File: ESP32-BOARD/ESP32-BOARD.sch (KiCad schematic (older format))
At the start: 160 parts, among them J101 Screw_Terminal_01x08, J102 Screw_Terminal_01x08, J103 Screw_Terminal_01x08, J104 Screw_Terminal_01x08, J105 Input_01x02, J106 Screw_Terminal_01x04, J120 Conn_01x07_Male, Q101 BT136-600, Q102 BT136-600, Q103 BT136-600, Q104 BT136-600, U101 LM358, U102 LM358, U103 LM2596S-ADJ, U104 LM2596S-ADJ, U105 TLP290-4, U106 TLP290-4, U107 KAQY214S, U108 KAQY214S, U109 MOC3023S, U110 MOC3023S, U111 MOC3023S, U112 MOC3023S, U113 SIM800L, U114 ESP32-dev-board

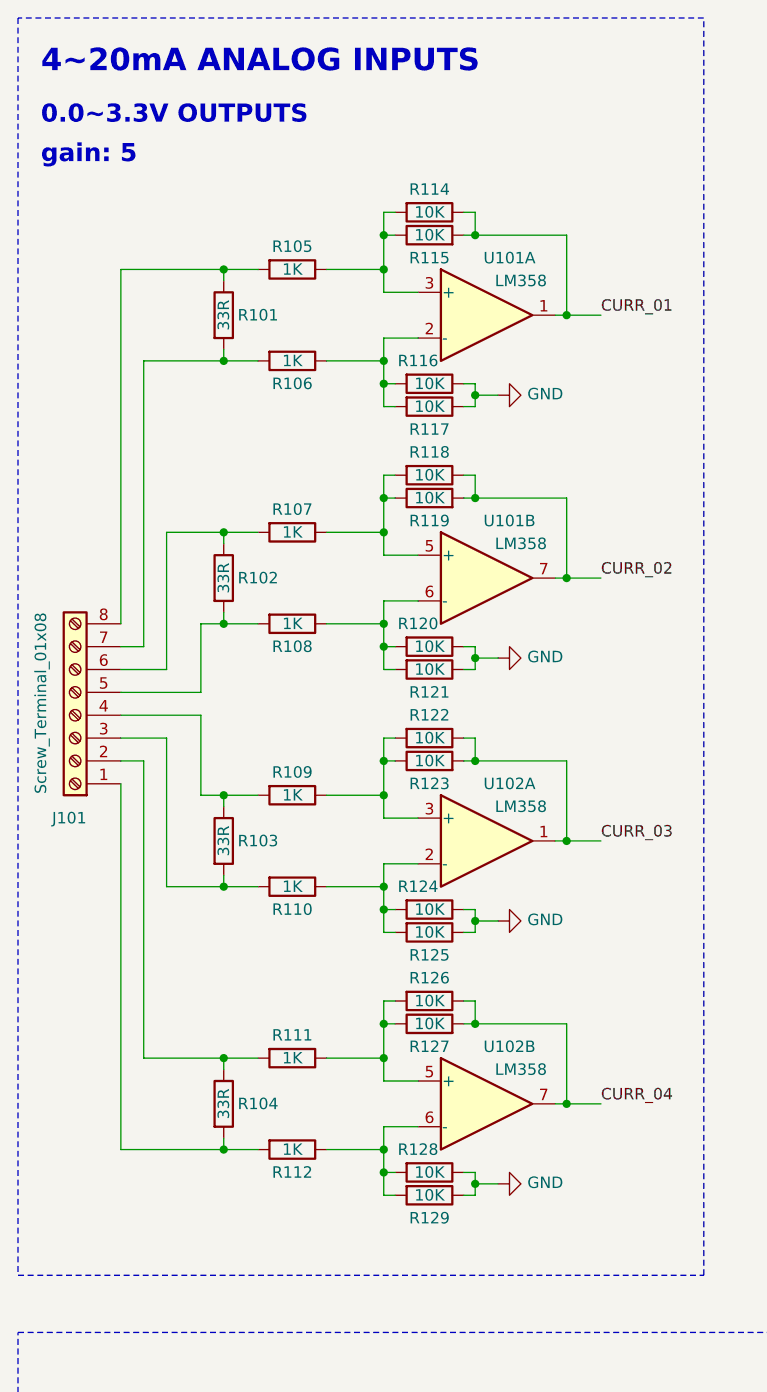
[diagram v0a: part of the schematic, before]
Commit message: changes made on the analog inputs
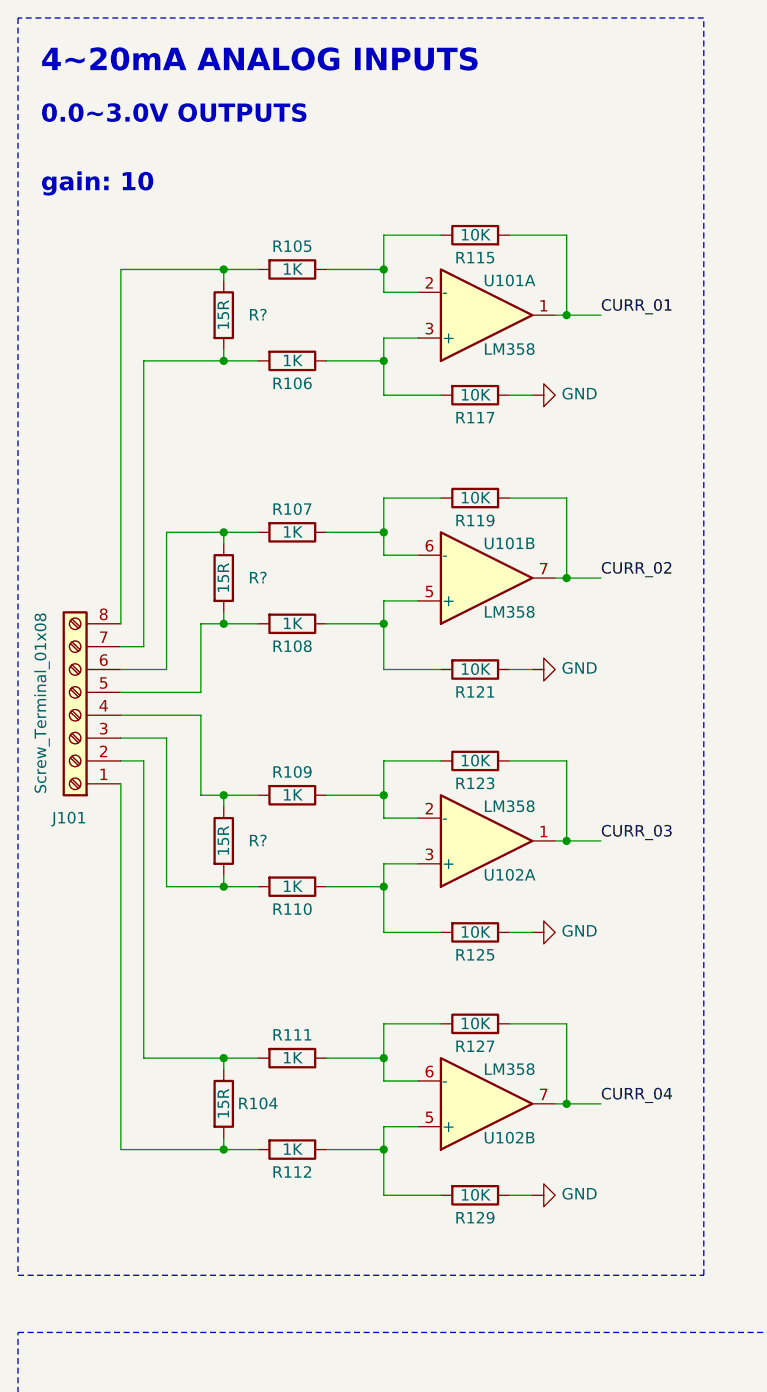
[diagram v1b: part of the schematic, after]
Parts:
- removed R101, R102, R103: 33R, Resistor_SMD:R_0805_2012Metric, symbol Device:R
- removed R114, R116, R118, R120, R122, R124, R126, R128: 10K, Resistor_SMD:R_0805_2012Metric, symbol Device:R
- added R? (x3): 15R, Resistor_SMD:R_0805_2012Metric, symbol Device:R
- R104: value 33R -> 15R; LCSC C17634 -> C17480
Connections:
- net at R106.1, R117.2: now also U101.3 (+); no longer U101.2 (-)
- net at R105.1, R115.1: now also U101.2 (-); no longer U101.3 (+)
- net at R107.1, R119.1: now also U101.6 (-); no longer U101.5 (+)
- net at R108.1, R121.2: now also U101.5 (+); no longer U101.6 (-)
- net at J101.8 (Pin_8), R105.2: now also R?.1
- net at J101.7 (Pin_7), R106.2: now also R?.2
- net at J101.6 (Pin_6), R107.2: now also R?.1
- net at J101.5 (Pin_5), R108.2: now also R?.2
- net at R110.1, R125.2: now also U102.3 (+); no longer U102.2 (-)
- net at R109.1, R123.1: now also U102.2 (-); no longer U102.3 (+)
- net at R111.1, R127.1: now also U102.6 (-); no longer U102.5 (+)
- net at R112.1, R129.2: now also U102.5 (+); no longer U102.6 (-)
- net at J101.4 (Pin_4), R109.2: now also R?.1
- net at J101.3 (Pin_3), R110.2: now also R?.2
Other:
- note added: "0.0~~3.0V OUTPUTS\n\n"
- note added: "gain: 10\n\n"
- note removed: "gain: 5\n\n\n"
- moved on the sheet: R115, R117, R119, R121, R123, R125, R127, R129

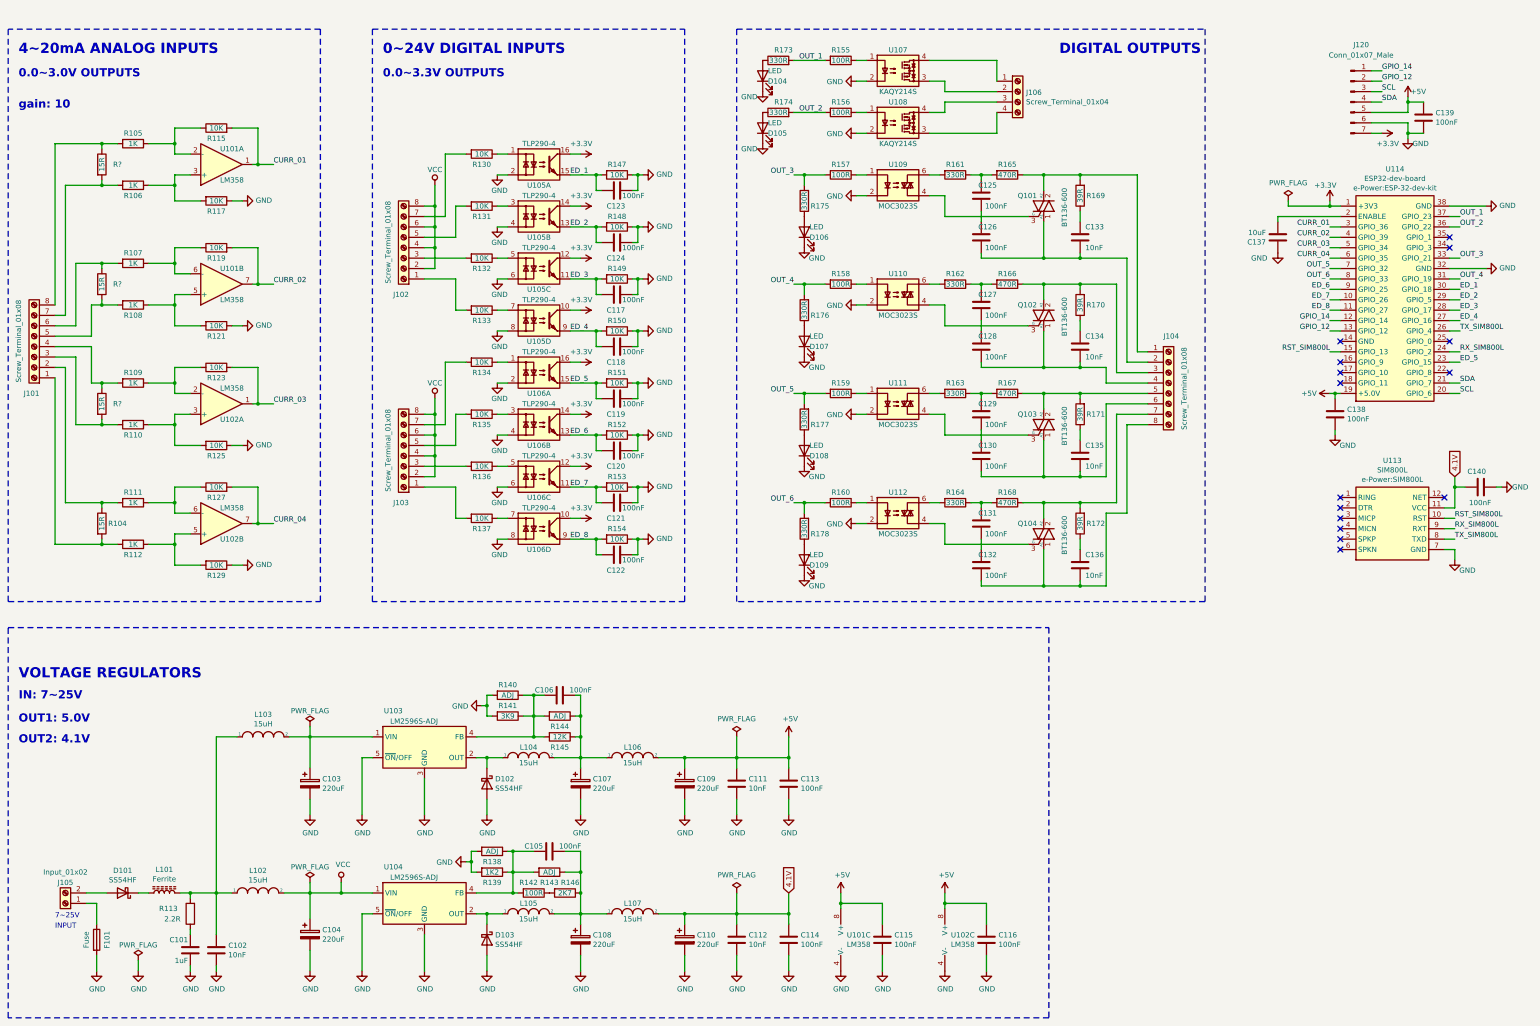
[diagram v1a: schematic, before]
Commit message: arrumei as dimensoes dos furos
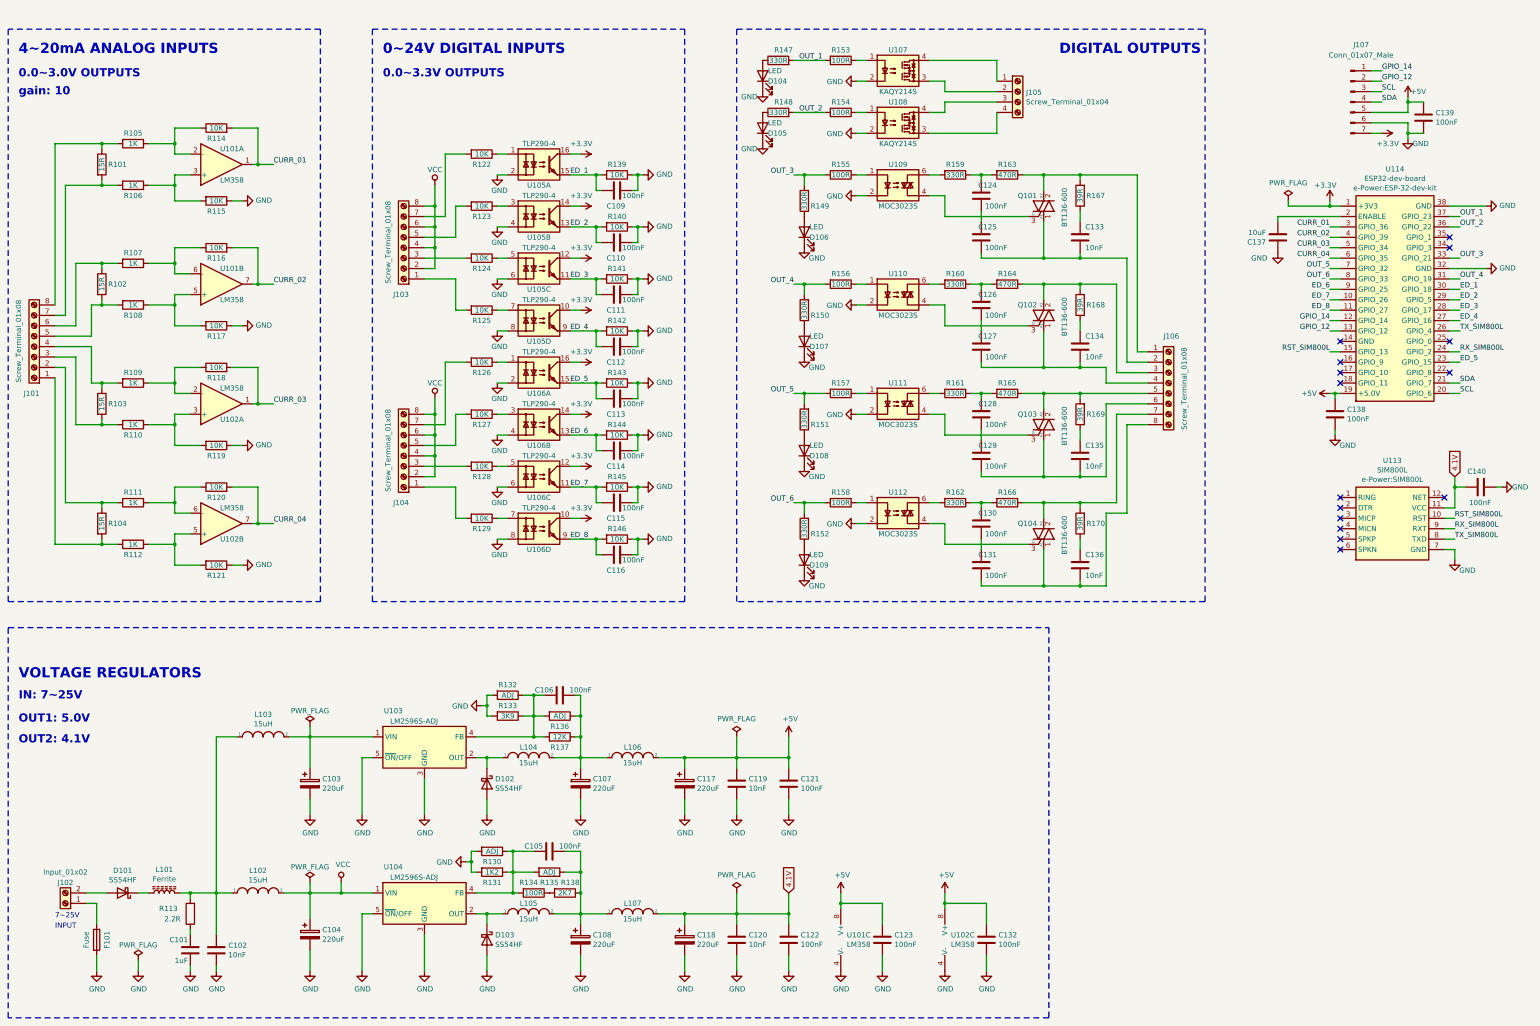
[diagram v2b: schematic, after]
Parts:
- gave numbers to parts that had none: 3
- renumbered C123 to C109, C124 to C110, C117 to C111, C118 to C112, C119 to C113, C120 to C114, C121 to C115, C122 to C116, C109 to C117, C110 to C118, C111 to C119, C112 to C120, C113 to C121, C114 to C122, C115 to C123, C125 to C124, C126 to C125, C127 to C126, C128 to C127, C129 to C128, C130 to C129, C131 to C130, C132 to C131, C116 to C132, J105 to J102, J102 to J103, J103 to J104, J106 to J105, J104 to J106, J120 to J107, R115 to R114, R117 to R115, R119 to R116, R121 to R117, R123 to R118, R125 to R119, R127 to R120, R129 to R121, R130 to R122, R131 to R123, R132 to R124, R133 to R125, R134 to R126, R135 to R127, R136 to R128, R137 to R129, R138 to R130, R139 to R131, R140 to R132, R141 to R133, R142 to R134, R143 to R135, R144 to R136, R145 to R137, R146 to R138, R147 to R139, R148 to R140, R149 to R141, R150 to R142, R151 to R143, R152 to R144, R153 to R145, R154 to R146, R173 to R147, R174 to R148, R175 to R149, R176 to R150, R177 to R151, R178 to R152, R155 to R153, R156 to R154, R157 to R155, R158 to R156, R159 to R157, R160 to R158, R161 to R159, R162 to R160, R163 to R161, R164 to R162, R165 to R163, R166 to R164, R167 to R165, R168 to R166, R169 to R167, R170 to R168, R171 to R169, R172 to R170
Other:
- note added: "gain: 10\n\n\n"
- note removed: "gain: 10\n\n"

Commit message: updates related to review B
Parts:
- added H101, H102, H103, H104: MountingHole_Pad, e-Power:MountingHole_4mm_Pad_Via, symbol Mechanical:MountingHole_Pad
- added H105: MountingHole_Pad, e-Power:MountingHole_3.2mm_M3_Pad, symbol Mechanical:MountingHole_Pad
- added R171: 0R, Resistor_SMD:R_0805_2012Metric, symbol Device:R
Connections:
- net +5V: now also R171.1; no longer C138.1, C139.1, J107.5 (Pin_5), U114.19 (+5.0V)
- net GND: now also H101.1, H102.1, H103.1, H104.1, H105.1
- new net 5V_u: C138.1, C139.1, J107.5 (Pin_5), R171.2, U114.19 (+5.0V)
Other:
- moved on the sheet: C138
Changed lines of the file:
@@
 L power:+5V #PWR0175
 U 1 1 5EF030E8
-P 13700 4500
-F 0 "#PWR0175" H 13700 4350 50  0001 C CNN
-F 1 "+5V" V 13700 4700 50  0000 C CNN
-F 2 "" H 13700 4500 50  0001 C CNN
-F 3 "" H 13700 4500 50  0001 C CNN
-	1    13700 4500
+P 13000 4500
+F 0 "#PWR0175" H 13000 4350 50  0001 C CNN
+F 1 "+5V" V 13000 4700 50  0000 C CNN
+F 2 "" H 13000 4500 50  0001 C CNN
+F 3 "" H 13000 4500 50  0001 C CNN
+	1    13000 4500
 	0    -1   -1   0
 $EndComp
-Wire Wire Line
-	13700 4500 13750 4500
 $Comp
 L power:+3.3V #PWR0174
@@
 $EndComp
 $Comp
-L power:+5V #PWR0178
-U 1 1 5F9DD3E9
-P 14450 1650
-F 0 "#PWR0178" H 14450 1500 50  0001 C CNN
-F 1 "+5V" H 14550 1700 50  0000 C CNN
-F 2 "" H 14450 1650 50  0001 C CNN
-F 3 "" H 14450 1650 50  0001 C CNN
-	1    14450 1650
-	1    0    0    -1
-$EndComp
-$Comp
 L power:GND #PWR0179
 U 1 1 5F9DE9D7
@@
 L Device:C C138
 U 1 1 5FA6F37C
-P 13750 4700
-F 0 "C138" H 13865 4746 50  0000 L CNN
-F 1 "100nF" H 13865 4655 50  0000 L CNN
-F 2 "Capacitor_SMD:C_0805_2012Metric" H 13788 4550 50  0001 C CNN
-F 3 "https://datasheet.lcsc.com/szlcsc/Samsung-Electro-Mechanics-CL21B103KBANNNC_C1710.pdf" H 13750 4700 50  0001 C CNN
-F 4 "C49678" H 13750 4700 50  0001 C CNN "LCSC"
-	1    13750 4700
-	1    0    0    -1
-$EndComp
-Wire Wire Line
-	13750 4550 13750 4500
-Connection ~ 13750 4500
-Wire Wire Line
-	13750 4500 13800 4500
+P 13500 4750
+F 0 "C138" H 13615 4796 50  0000 L CNN
+F 1 "100nF" H 13615 4705 50  0000 L CNN
+F 2 "Capacitor_SMD:C_0805_2012Metric" H 13538 4600 50  0001 C CNN
+F 3 "https://datasheet.lcsc.com/szlcsc/Samsung-Electro-Mechanics-CL21B103KBANNNC_C1710.pdf" H 13500 4750 50  0001 C CNN
+F 4 "C49678" H 13500 4750 50  0001 C CNN "LCSC"
+	1    13500 4750
+	1    0    0    -1
+$EndComp
+Connection ~ 13500 4500
 $Comp
 L Device:C C139
@@
 L power:GND #PWR0176
 U 1 1 5FBD44B2
-P 13750 4900
-F 0 "#PWR0176" H 13750 4650 50  0001 C CNN
-F 1 "GND" H 13950 4800 50  0000 R CNN
-F 2 "" H 13750 4900 50  0001 C CNN
-F 3 "" H 13750 4900 50  0001 C CNN
-	1    13750 4900
-	1    0    0    -1
-$EndComp
-Wire Wire Line
-	13750 4900 13750 4850
+P 13500 4950
+F 0 "#PWR0176" H 13500 4700 50  0001 C CNN
+F 1 "GND" H 13700 4850 50  0000 R CNN
+F 2 "" H 13500 4950 50  0001 C CNN
+F 3 "" H 13500 4950 50  0001 C CNN
+	1    13500 4950
+	1    0    0    -1
+$EndComp
+Wire Wire Line
+	13500 4950 13500 4900
 $Comp
 L power:GND #PWR0180
@@
 Text Notes 1100 1900 0    79   ~ 16
 gain: 10\n\n\n
+$Comp
+L Mechanical:MountingHole_Pad H101
+U 1 1 5F271E78
+P 9000 8000
+F 0 "H101" H 8950 8200 50  0000 L CNN
+F 1 "MountingHole_Pad" H 9100 7958 50  0001 L CNN
+F 2 "e-Power:MountingHole_4mm_Pad_Via" H 9000 8000 50  0001 C CNN
+F 3 "~" H 9000 8000 50  0001 C CNN
+	1    9000 8000
+	1    0    0    -1
+$EndComp
+$Comp
+L Mechanical:MountingHole_Pad H102
+U 1 1 5F272A66
+P 9200 8000
+F 0 "H102" H 9150 8200 50  0000 L CNN
+F 1 "MountingHole_Pad" H 9300 7958 50  0001 L CNN
+F 2 "e-Power:MountingHole_4mm_Pad_Via" H 9200 8000 50  0001 C CNN
+F 3 "~" H 9200 8000 50  0001 C CNN
+	1    9200 8000
+	1    0    0    -1
+$EndComp
+$Comp
+L Mechanical:MountingHole_Pad H103
+U 1 1 5F2734E8
+P 9400 8000
+F 0 "H103" H 9350 8200 50  0000 L CNN
+F 1 "MountingHole_Pad" H 9500 7958 50  0001 L CNN
+F 2 "e-Power:MountingHole_4mm_Pad_Via" H 9400 8000 50  0001 C CNN
+F 3 "~" H 9400 8000 50  0001 C CNN
+	1    9400 8000
+	1    0    0    -1
+$EndComp
+$Comp
+L Mechanical:MountingHole_Pad H104
+U 1 1 5F273752
+P 9600 8000
+F 0 "H104" H 9550 8200 50  0000 L CNN
+F 1 "MountingHole_Pad" H 9700 7958 50  0001 L CNN
+F 2 "e-Power:MountingHole_4mm_Pad_Via" H 9600 8000 50  0001 C CNN
+F 3 "~" H 9600 8000 50  0001 C CNN
+	1    9600 8000
+	1    0    0    -1
+$EndComp
+$Comp
+L power:GND #PWR0184
+U 1 1 5F273931
+P 9000 8250
+F 0 "#PWR0184" H 9000 8000 50  0001 C CNN
+F 1 "GND" H 9005 8077 50  0000 C CNN
+F 2 "" H 9000 8250 50  0001 C CNN
+F 3 "" H 9000 8250 50  0001 C CNN
+	1    9000 8250
+	1    0    0    -1
+$EndComp
+Wire Wire Line
+	9000 8250 9000 8200
+Wire Wire Line
+	9000 8200 9200 8200
+Wire Wire Line
+	9600 8200 9600 8100
+Connection ~ 9000 8200
+Wire Wire Line
+	9000 8200 9000 8100
+Wire Wire Line
+	9400 8100 9400 8200
+Connection ~ 9400 8200
+Wire Wire Line
+	9400 8200 9600 8200
+Wire Wire Line
+	9200 8100 9200 8200
+Connection ~ 9200 8200
+Wire Wire Line
+	9200 8200 9400 8200
+$Comp
+L Mechanical:MountingHole_Pad H105
+U 1 1 5F4C024E
+P 10000 8000
+F 0 "H105" H 9950 8200 50  0000 L CNN
+F 1 "MountingHole_Pad" H 10100 7958 50  0001 L CNN
+F 2 "e-Power:MountingHole_3.2mm_M3_Pad" H 10000 8000 50  0001 C CNN
+F 3 "~" H 10000 8000 50  0001 C CNN
+	1    10000 8000
+	1    0    0    -1
+$EndComp
+$Comp
+L power:GND #PWR0185
+U 1 1 5F4C08F3
+P 10000 8250
+F 0 "#PWR0185" H 10000 8000 50  0001 C CNN
+F 1 "GND" H 10005 8077 50  0000 C CNN
+F 2 "" H 10000 8250 50  0001 C CNN
+F 3 "" H 10000 8250 50  0001 C CNN
+	1    10000 8250
+	1    0    0    -1
+$EndComp
+Wire Wire Line
+	10000 8250 10000 8100
+$Comp
+L Device:R R171
+U 1 1 5F574CA2
+P 13250 4500
+F 0 "R171" V 13350 4500 50  0000 C CNN
+F 1 "0R" V 13250 4500 50  0000 C CNN
+F 2 "Resistor_SMD:R_0805_2012Metric" V 13180 4500 50  0001 C CNN
+F 3 "" H 13250 4500 50  0001 C CNN
+F 4 "C17477" H 13250 4500 50  0001 C CNN "LCSC"
+	1    13250 4500
+	0    -1   -1   0
+$EndComp
+Wire Wire Line
+	13000 4500 13100 4500
+Wire Wire Line
+	13400 4500 13500 4500
+Wire Wire Line
+	13500 4500 13500 4600
+Text Label 13600 4500 0    50   ~ 0
+5V_u
+Wire Wire Line
+	13500 4500 13800 4500
+Text Label 14450 1650 0    50   ~ 0
+5V_u
 $EndSCHEMATC

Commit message: added 3d models
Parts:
- C103, C104, C107, C108, C117, C118: LCSC C134765 -> C311611
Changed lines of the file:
@@
 Sheet 1 1
 Title "ESP32-BOARD"
-Date ""
-Rev "REV0"
+Date "2020-07-27"
+Rev "REV. B"
 Comp "Gabriel Gosmann"
 Comment1 ""
@@
 F 2 "Capacitor_SMD:CP_Elec_8x10" H 3938 9550 50  0001 C CNN
 F 3 "https://datasheet.lcsc.com/szlcsc/Lelon-VE-471M1E1010-TR0_C249931.pdf" H 3900 9700 50  0001 C CNN
-F 4 "C134765" H 3900 9700 50  0001 C CNN "LCSC"
+F 4 "C311611" H 3900 9700 50  0001 C CNN "LCSC"
 	1    3900 9700
 	1    0    0    -1
@@
 F 2 "Capacitor_SMD:CP_Elec_8x10" H 3938 8100 50  0001 C CNN
 F 3 "https://datasheet.lcsc.com/szlcsc/Lelon-VE-471M1E1010-TR0_C249931.pdf" H 3900 8250 50  0001 C CNN
-F 4 "C134765" H 3900 8250 50  0001 C CNN "LCSC"
+F 4 "C311611" H 3900 8250 50  0001 C CNN "LCSC"
 	1    3900 8250
 	1    0    0    -1
@@
 F 2 "Capacitor_SMD:CP_Elec_8x10" H 6538 8100 50  0001 C CNN
 F 3 "https://datasheet.lcsc.com/szlcsc/Lelon-VES221M1CTR-0607_C127327.pdf" H 6500 8250 50  0001 C CNN
-F 4 "C134765" H 6500 8250 50  0001 C CNN "LCSC"
+F 4 "C311611" H 6500 8250 50  0001 C CNN "LCSC"
 	1    6500 8250
 	1    0    0    -1
@@
 F 2 "Capacitor_SMD:CP_Elec_8x10" H 6538 9600 50  0001 C CNN
 F 3 "https://datasheet.lcsc.com/szlcsc/Lelon-VES221M1CTR-0607_C127327.pdf" H 6500 9750 50  0001 C CNN
-F 4 "C134765" H 6500 9750 50  0001 C CNN "LCSC"
+F 4 "C311611" H 6500 9750 50  0001 C CNN "LCSC"
 	1    6500 9750
 	1    0    0    -1
@@
 F 2 "Capacitor_SMD:CP_Elec_8x10" H 7538 9600 50  0001 C CNN
 F 3 "https://datasheet.lcsc.com/szlcsc/Lelon-VE-471M1E1010-TR0_C249931.pdf" H 7500 9750 50  0001 C CNN
-F 4 "C134765" H 7500 9750 50  0001 C CNN "LCSC"
+F 4 "C311611" H 7500 9750 50  0001 C CNN "LCSC"
 	1    7500 9750
 	1    0    0    -1
@@
 F 2 "Capacitor_SMD:CP_Elec_8x10" H 7538 8100 50  0001 C CNN
 F 3 "https://datasheet.lcsc.com/szlcsc/Lelon-VE-471M1E1010-TR0_C249931.pdf" H 7500 8250 50  0001 C CNN
-F 4 "C134765" H 7500 8250 50  0001 C CNN "LCSC"
+F 4 "C311611" H 7500 8250 50  0001 C CNN "LCSC"
 	1    7500 8250
 	1    0    0    -1
